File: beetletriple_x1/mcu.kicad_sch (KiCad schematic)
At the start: 17 parts, among them J10 soicbite programming connector, J5 input_c1, J6 input_c2, J7 input_c3, J8 output_c4, J9 output_c5, U3 ATtiny1617-M

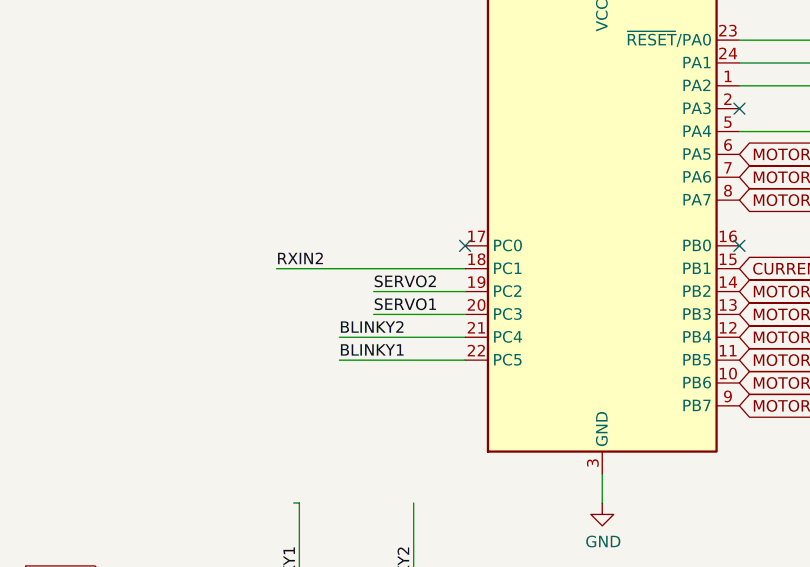
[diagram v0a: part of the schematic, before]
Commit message: Beetletriple version x1 with the dfn-8 gate driver finally fix up routing and errors
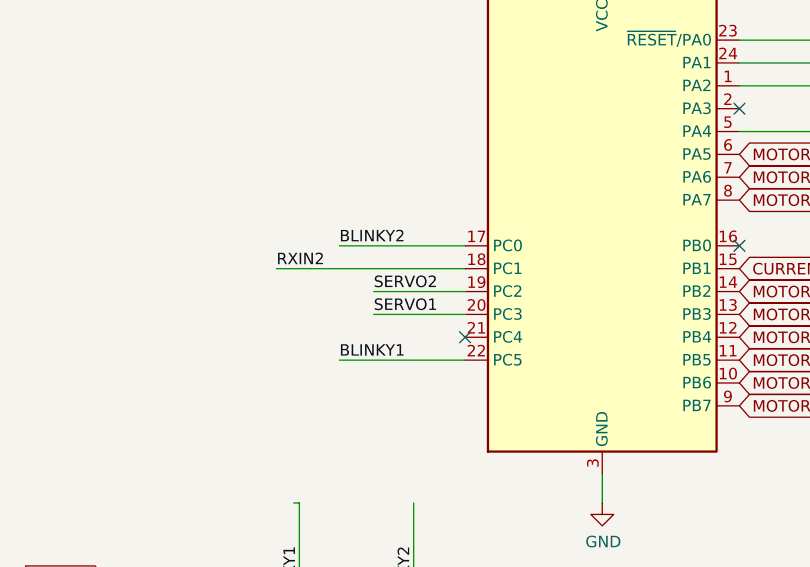
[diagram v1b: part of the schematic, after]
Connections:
- net BLINKY2: now also U3.17 (PC0); no longer U3.21 (PC4)
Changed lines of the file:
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@@
   (junction (at 220.345 116.84) (diameter 0.9144) (color 0 0 0 0))
   (junction (at 225.425 98.425) (diameter 0.9144) (color 0 0 0 0))
-  (no_connect (at 114.3 104.14))
+  (no_connect (at 114.3 114.3))
   (no_connect (at 144.78 88.9))
   (no_connect (at 144.78 104.14))
@@
     (stroke (width 0) (type solid) (color 0 0 0 0))
   )
-  (wire (pts (xy 100.33 114.3) (xy 114.3 114.3))
+  (wire (pts (xy 100.33 104.14) (xy 114.3 104.14))
     (stroke (width 0) (type solid) (color 0 0 0 0))
   )
@@
     (effects (font (size 1.27 1.27)) (justify left bottom))
   )
-  (label "BLINKY2" (at 100.33 114.3 0)
-    (effects (font (size 1.27 1.27)) (justify left bottom))
-  )
+  (label "BLINKY2" (at 100.33 104.14 0)
+    (effects (font (size 1.27 1.27)) (justify left bottom))
+  )

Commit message: Footprints shenanigans
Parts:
- U3: footprint Package_DFN_QFN:QFN-24-1EP_4x4mm_P0.5mm_EP2.6x2.6mm -> beetletriple:qfn24-hand1
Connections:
- net RXIN2: now also U3.19 (PC2); no longer U3.18 (PC1)
- net SERVO2: now also U3.18 (PC1); no longer U3.19 (PC2)
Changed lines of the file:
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@@
+    (stroke (width 0) (type solid) (color 0 0 0 0))
+  )
+  (wire (pts (xy 104.775 106.68) (xy 114.3 106.68))
     (stroke (width 0) (type solid) (color 0 0 0 0))
   )
@@
     (stroke (width 0) (type solid) (color 0 0 0 0))
   )
-  (wire (pts (xy 114.3 106.68) (xy 93.345 106.68))
-    (stroke (width 0) (type solid) (color 0 0 0 0))
-  )
   (wire (pts (xy 129.54 57.15) (xy 129.54 73.66))
     (stroke (width 0) (type solid) (color 0 0 0 0))
@@
     (effects (font (size 1.27 1.27)) (justify right bottom))
   )
-  (label "RXIN2" (at 93.345 106.68 0)
-    (effects (font (size 1.27 1.27)) (justify left bottom))
-  )
   (label "BLINKY1" (at 95.885 144.78 90)
     (effects (font (size 1.27 1.27)) (justify left bottom))
@@
     (effects (font (size 1.27 1.27)) (justify left bottom))
   )
-  (label "SERVO2" (at 104.14 109.22 0)
+  (label "RXIN2" (at 104.14 109.22 0)
     (effects (font (size 1.27 1.27)) (justify left bottom))
   )
   (label "SERVO1" (at 104.14 111.76 0)
+    (effects (font (size 1.27 1.27)) (justify left bottom))
+  )
+  (label "SERVO2" (at 104.775 106.68 0)
     (effects (font (size 1.27 1.27)) (justify left bottom))
   )
@@
     (property "Reference" "U3" (id 0) (at 133.35 71.1008 0))
     (property "Value" "ATtiny1617-M" (id 1) (at 139.065 74.0345 0))
-    (property "Footprint" "Package_DFN_QFN:QFN-24-1EP_4x4mm_P0.5mm_EP2.6x2.6mm" (id 2) (at 129.54 101.6 0)
+    (property "Footprint" "beetletriple:qfn24-hand1" (id 2) (at 129.54 101.6 0)
       (effects (font (size 1.27 1.27) italic) hide)
     )
